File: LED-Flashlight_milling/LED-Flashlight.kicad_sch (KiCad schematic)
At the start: 10 parts, among them IC1 TLV61220, SW1 SW_SKRPABE010

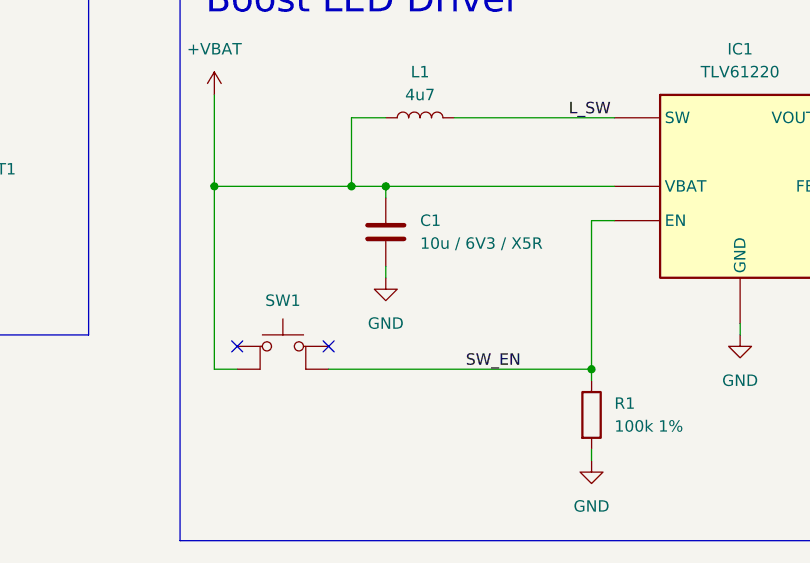
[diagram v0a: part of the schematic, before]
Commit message: added milling files, lib changes, added footprint tables, changed to kicad 10 format
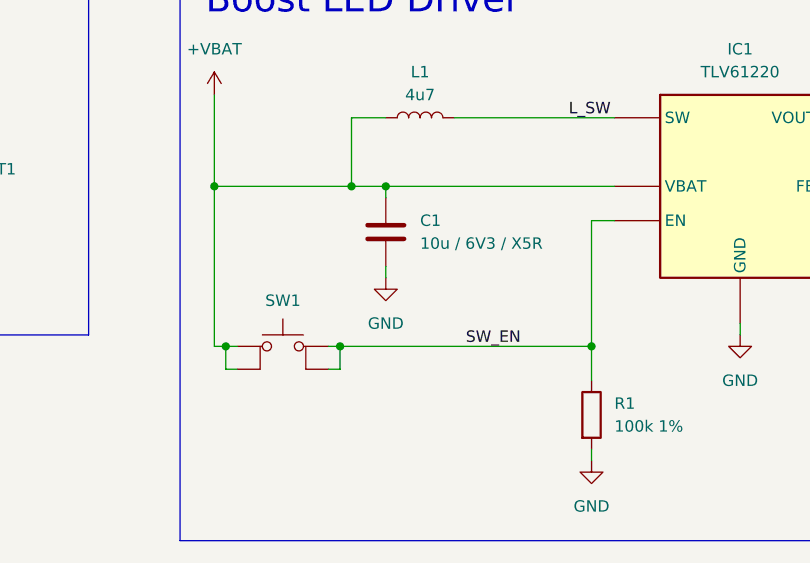
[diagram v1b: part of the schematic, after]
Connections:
- net +VBAT: now also SW1.1
- net SW_EN: now also SW1.4 (A)
- no-connect marks 2 -> 0
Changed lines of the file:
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@@
+	)
+	(junction
+		(at 177.8 93.98)
+		(diameter 0)
+		(color 0 0 0 0)
+	)
+	(junction
+		(at 203.2 114.3)
+		(diameter 0)
+		(color 0 0 0 0)
+	)
+	(junction
+		(at 138.43 119.38)
+		(diameter 0)
+		(color 0 0 0 0)
 	)
 	(junction
@@
 	)
 	(junction
-		(at 177.8 93.98)
-		(diameter 0)
-		(color 0 0 0 0)
-	)
-	(junction
-		(at 138.43 121.92)
-		(diameter 0)
-		(color 0 0 0 0)
-	)
-	(junction
-		(at 203.2 114.3)
-		(diameter 0)
-		(color 0 0 0 0)
-	)
-	(junction
 		(at 115.57 101.6)
 		(diameter 0)
@@
 	)
 	(junction
+		(at 110.49 119.38)
+		(diameter 0)
+		(color 0 0 0 0)
+	)
+	(junction
+		(at 97.79 119.38)
+		(diameter 0)
+		(color 0 0 0 0)
+	)
+	(junction
 		(at 111.76 101.6)
 		(diameter 0)
@@
 		(color 0 0 0 0)
 	)
-	(no_connect
-		(at 109.22 119.38)
-	)
-	(no_connect
-		(at 99.06 119.38)
-	)
 	(wire
 		(pts
@@
 	(wire
 		(pts
+			(xy 110.49 119.38) (xy 110.49 121.92)
+		)
+		(stroke
+			(width 0)
+			(type default)
+		)
+	)
+	(wire
+		(pts
 			(xy 111.76 101.6) (xy 96.52 101.6)
 		)
@@
 	(wire
 		(pts
+			(xy 110.49 119.38) (xy 138.43 119.38)
+		)
+		(stroke
+			(width 0)
+			(type default)
+		)
+	)
+	(wire
+		(pts
 			(xy 111.76 93.98) (xy 111.76 101.6)
 		)
@@
 	(wire
 		(pts
+			(xy 99.06 121.92) (xy 97.79 121.92)
+		)
+		(stroke
+			(width 0)
+			(type default)
+		)
+	)
+	(wire
+		(pts
 			(xy 168.91 101.6) (xy 173.99 101.6)
 		)
@@
 	(wire
 		(pts
-			(xy 138.43 105.41) (xy 138.43 121.92)
+			(xy 138.43 119.38) (xy 138.43 105.41)
 		)
 		(stroke
@@
 	(wire
 		(pts
+			(xy 99.06 119.38) (xy 97.79 119.38)
+		)
+		(stroke
+			(width 0)
+			(type default)
+		)
+	)
+	(wire
+		(pts
 			(xy 177.8 93.98) (xy 203.2 93.98)
 		)
@@
 	(wire
 		(pts
+			(xy 109.22 121.92) (xy 110.49 121.92)
+		)
+		(stroke
+			(width 0)
+			(type default)
+		)
+	)
+	(wire
+		(pts
 			(xy 173.99 114.3) (xy 203.2 114.3)
 		)
@@
 	(wire
 		(pts
-			(xy 109.22 121.92) (xy 138.43 121.92)
-		)
-		(stroke
-			(width 0)
-			(type default)
-		)
-	)
-	(wire
-		(pts
-			(xy 138.43 123.19) (xy 138.43 121.92)
-		)
-		(stroke
-			(width 0)
-			(type default)
-		)
-	)
-	(wire
-		(pts
-			(xy 96.52 121.92) (xy 96.52 101.6)
-		)
-		(stroke
-			(width 0)
-			(type default)
-		)
-	)
-	(wire
-		(pts
-			(xy 96.52 121.92) (xy 99.06 121.92)
+			(xy 97.79 119.38) (xy 97.79 121.92)
+		)
+		(stroke
+			(width 0)
+			(type default)
+		)
+	)
+	(wire
+		(pts
+			(xy 109.22 119.38) (xy 110.49 119.38)
+		)
+		(stroke
+			(width 0)
+			(type default)
+		)
+	)
+	(wire
+		(pts
+			(xy 138.43 123.19) (xy 138.43 119.38)
+		)
+		(stroke
+			(width 0)
+			(type default)
+		)
+	)
+	(wire
+		(pts
+			(xy 96.52 119.38) (xy 96.52 101.6)
+		)
+		(stroke
+			(width 0)
+			(type default)
+		)
+	)
+	(wire
+		(pts
+			(xy 97.79 119.38) (xy 96.52 119.38)
 		)
 		(stroke
@@
 	)
 	(label "SW_EN"
-		(at 124.46 121.92 0)
+		(at 124.46 119.38 0)
 		(effects
 			(font
@@
 			)
 		)
-		(property ".SCH_Checked" ""
-			(at 96.52 91.44 0)
-			(hide yes)
-			(show_name no)
-			(do_not_autoplace no)
-			(effects
-				(font
-					(size 1.27 1.27)
-				)
-			)
-		)
-		(property "Supplier1" ""
-			(at 96.52 91.44 0)
-			(hide yes)
-			(show_name no)
-			(do_not_autoplace no)
-			(effects
-				(font
-					(size 1.27 1.27)
-				)
-			)
-		)
-		(property "Supplier1_Part_No" ""
-			(at 96.52 91.44 0)
-			(hide yes)
-			(show_name no)
-			(do_not_autoplace no)
-			(effects
-				(font
-					(size 1.27 1.27)
-				)
-			)
-		)
-		(property "Manufacturer" ""
-			(at 96.52 91.44 0)
-			(hide yes)
-			(show_name no)
-			(do_not_autoplace no)
-			(effects
-				(font
-					(size 1.27 1.27)
-				)
-			)
-		)
-		(property "Manufacturer_Part_No" ""
-			(at 96.52 91.44 0)
-			(hide yes)
-			(show_name no)
-			(do_not_autoplace no)
-			(effects
-				(font
-					(size 1.27 1.27)
-				)
-			)
-		)
-		(property "Category" ""
-			(at 96.52 91.44 0)
-			(hide yes)
-			(show_name no)
-			(do_not_autoplace no)
-			(effects
-				(font
-					(size 1.27 1.27)
-				)
-			)
-		)
-		(property ".PCB_Checked" ""
-			(at 96.52 91.44 0)
-			(hide yes)
-			(show_name no)
-			(do_not_autoplace no)
-			(effects
-				(font
-					(size 1.27 1.27)
-				)
-			)
-		)
 		(pin "1"
 		)
@@
 			(at 67.31 91.44 0)
 			(hide yes)
-			(show_name no)
-			(do_not_autoplace no)
-			(effects
-				(font
-					(size 1.27 1.27)
-				)
-			)
-		)
-		(property ".SCH_Checked" ""
-			(at 67.31 91.44 0)
-			(hide yes)
-			(show_name no)
-			(do_not_autoplace no)
-			(effects
-				(font
-					(size 1.27 1.27)
-				)
-			)
-		)
-		(property "Supplier1" ""
-			(at 67.31 91.44 0)
-			(hide yes)
-			(show_name no)
-			(do_not_autoplace no)
-			(effects
-				(font
-					(size 1.27 1.27)
-				)
-			)
-		)
-		(property "Supplier1_Part_No" ""
-			(at 67.31 91.44 0)
-			(hide yes)
-			(show_name no)
-			(do_not_autoplace no)
-			(effects
-				(font
-					(size 1.27 1.27)
-				)
-			)
-		)
-		(property "Manufacturer" ""
-			(at 67.31 91.44 0)
-			(hide yes)
-			(show_name no)
-			(do_not_autoplace no)
-			(effects
-				(font
-					(size 1.27 1.27)
-				)
-			)
-		)
-		(property "Manufacturer_Part_No" ""
-			(at 67.31 91.44 0)
-			(hide yes)
-			(show_name no)
-			(do_not_autoplace no)
-			(effects
-				(font
-					(size 1.27 1.27)
-				)
-			)
-		)
-		(property "Category" ""
-			(at 67.31 91.44 0)
-			(hide yes)
-			(show_name no)
-			(do_not_autoplace no)
-			(effects
-				(font
-					(size 1.27 1.27)
-				)
-			)
-		)
-		(property ".PCB_Checked" ""
-			(at 67.31 91.44 0)
-			(hide yes)
